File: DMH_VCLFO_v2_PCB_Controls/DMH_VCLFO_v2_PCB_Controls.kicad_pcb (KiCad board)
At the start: 2 copper layers, 98 x 120.5 mm, 67 parts, among them J19 Conn_01x08, J20 Conn_01x08, J24 Conn_01x08, J25 Conn_01x08, J29 Conn_01x08, J30 Conn_01x08, J54 Conn_01x06, Q1 BC548, Q2 BC558, Q3 BC548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

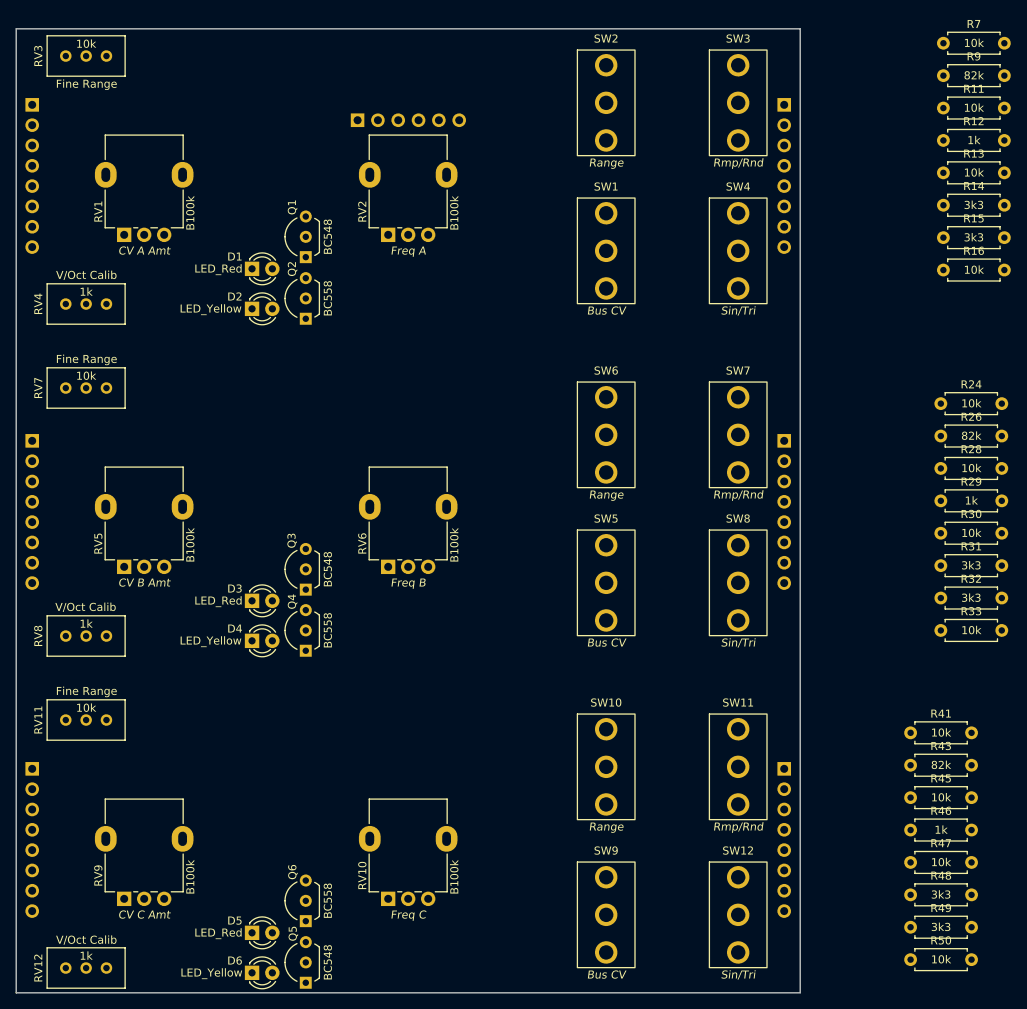
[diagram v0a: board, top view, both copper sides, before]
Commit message: Controls PCB routing done
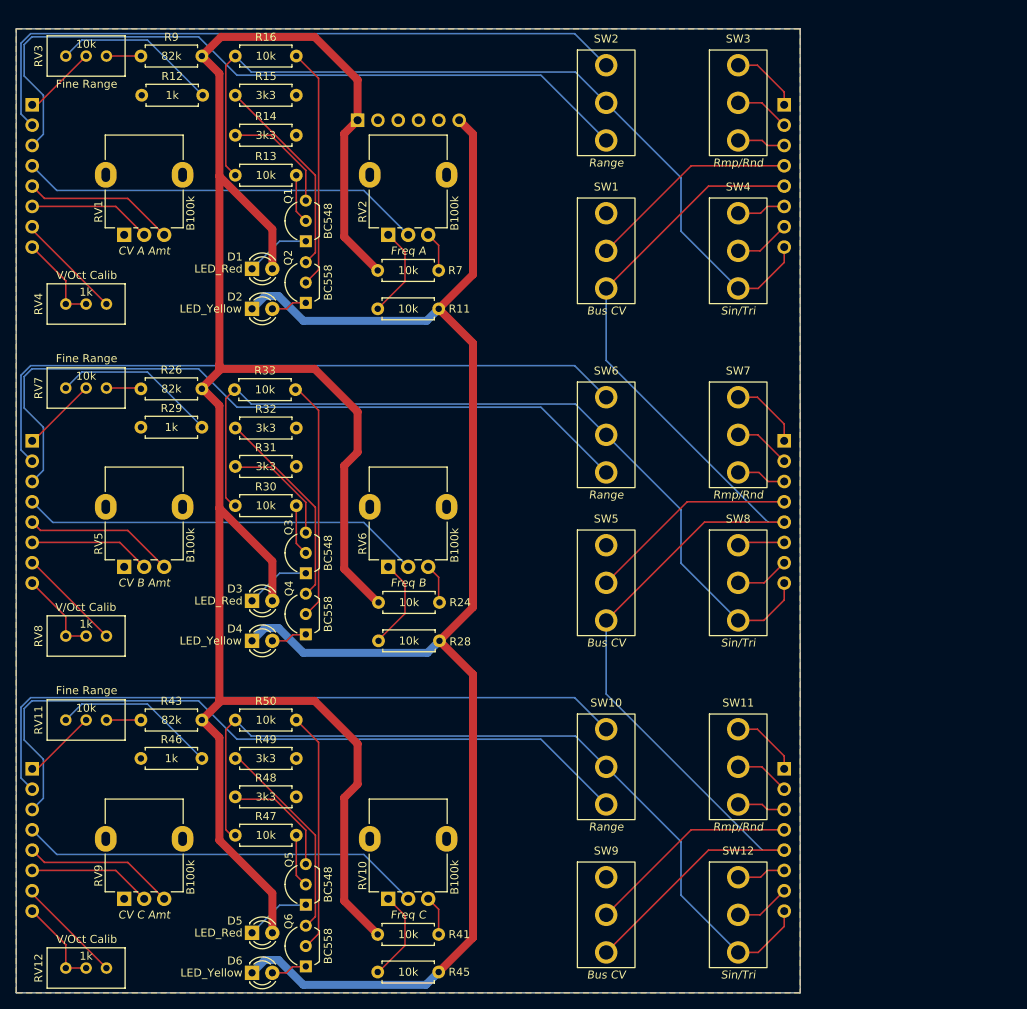
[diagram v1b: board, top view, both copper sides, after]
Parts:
- moved R29 100.4 mm to (66.6, 92.3)
- moved R12 100.4 mm to (66.7, 50.8)
- moved R9 100.3 mm to (66.6, 45.9)
- moved R26 100.2 mm to (66.6, 87.5)
- moved R46 96.6 mm to (66.6, 133.7)
- moved R43 96.4 mm to (66.6, 128.9)
- moved R33 93.3 mm to (78.3, 87.6)
- moved R16 92.5 mm to (78.4, 45.9)
- moved R32 90.7 mm to (78.4, 92.4)
- moved R15 90.3 mm to (78.4, 50.8)
- moved R50 89.6 mm to (78.4, 128.9)
- moved R31 89.1 mm to (78.4, 97.2)
- moved R14 88.9 mm to (78.4, 55.8)
- moved R13 88.5 mm to (78.4, 60.8)
- moved R30 88.3 mm to (78.4, 102.1)
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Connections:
- J19 pad 1: A_Rng_Sw_p1_C -> A_FRng_Trim_p2_C
- J19 pad 3: A_Freq_Pot_p2_C -> A_Rng_Sw_p1_C
- J19 pad 4: A_CV_Amt_Pot_p2_C -> A_Freq_Pot_p2_C
- J19 pad 6: A_FRng_Trim_p2_C -> A_CV_Amt_Pot_p2_C
- J19 pad 7: A_VOct_Trim_p12_C -> A_VOct_Trim_p3_C
- J19 pad 8: A_VOct_Trim_p3_C -> A_VOct_Trim_p12_C
- J20 pad 4: A_Sin_C -> A_BusCV_Sw_p2_C
- J20 pad 5: A_Sin_Tri_Sw_p2_C -> Bus_CV_C
- J20 pad 6: A_Tri_C -> A_Sin_C
- J20 pad 7: A_BusCV_Sw_p2_C -> A_Sin_Tri_Sw_p2_C
- J20 pad 8: Bus_CV_C -> A_Tri_C
- J24 pad 1: B_Rng_Sw_p1_C -> B_FRng_Trim_p2_C
- J24 pad 3: B_Freq_Pot_p2_C -> B_Rng_Sw_p1_C
- J24 pad 4: B_CV_Amt_Pot_p2_C -> B_Freq_Pot_p2_C
- J24 pad 6: B_FRng_Trim_p2_C -> B_CV_Amt_Pot_p2_C
- J24 pad 7: B_VOct_Trim_p12_C -> B_VOct_Trim_p3_C
- J24 pad 8: B_VOct_Trim_p3_C -> B_VOct_Trim_p12_C
- J25 pad 4: B_Sin_C -> B_BusCV_Sw_p2_C
- J25 pad 5: B_Sin_Tri_Sw_p2_C -> Bus_CV_C
- J25 pad 6: B_Tri_C -> B_Sin_C
- J25 pad 7: B_BusCV_Sw_p2_C -> B_Sin_Tri_Sw_p2_C
- J25 pad 8: Bus_CV_C -> B_Tri_C
- J29 pad 1: C_Rng_Sw_p1_C -> C_FRng_Trim_p2_C
- J29 pad 3: C_Freq_Pot_p2_C -> C_Rng_Sw_p1_C
- J29 pad 4: C_CV_Amt_Pot_p2_C -> C_Freq_Pot_p2_C
- J29 pad 6: C_FRng_Trim_p2_C -> C_CV_Amt_Pot_p2_C
- J29 pad 7: C_VOct_Trim_p12_C -> C_VOct_Trim_p3_C
- J29 pad 8: C_VOct_Trim_p3_C -> C_VOct_Trim_p12_C
- J30 pad 4: C_Sin_C -> C_BusCV_Sw_p2_C
- J30 pad 5: C_Sin_Tri_Sw_p2_C -> Bus_CV_C
- J30 pad 6: C_Tri_C -> C_Sin_C
- J30 pad 7: C_BusCV_Sw_p2_C -> C_Sin_Tri_Sw_p2_C
- J30 pad 8: Bus_CV_C -> C_Tri_C
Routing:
- net +12V: track 0.00 -> 286.5 mm
- net -12V: track 0.00 -> 193.8 mm
- net Bus_CV_C: track 0.00 -> 161.6 mm
- net B_Tri_C: track 0.00 -> 104.1 mm
- net A_Tri_C: track 0.00 -> 103.7 mm
- net C_Tri_C: track 0.00 -> 103.7 mm
- net B_Rng_Sw_p1_C: track 0.00 -> 93.2 mm
- net A_Rng_Sw_p1_C: track 0.00 -> 92.8 mm
- net C_Rng_Sw_p1_C: track 0.00 -> 92.8 mm
- net B_Rng_Sw_p3_C: track 0.00 -> 86.6 mm
- net A_Rng_Sw_p3_C: track 0.00 -> 86.1 mm
- net C_Rng_Sw_p3_C: track 0.00 -> 86.1 mm
- net C_Freq_Pot_p2_C: track 0.00 -> 50.6 mm
- net A_Freq_Pot_p2_C: track 0.00 -> 50.6 mm
- net B_Freq_Pot_p2_C: track 0.00 -> 50.4 mm
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- added copper zone on B.Cu, net GND
- added copper zone on F.Cu, net GND

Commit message: Generated Gerbers
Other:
- board text added: "Mk1.0 - March 2026"
- board text removed: "Mk1.0 - Month Year"
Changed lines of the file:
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@@
 			(plot_on_all_layers_selection 0x00000000_00000000_00000000_00000000)
 			(disableapertmacros no)
-			(usegerberextensions no)
+			(usegerberextensions yes)
 			(usegerberattributes yes)
 			(usegerberadvancedattributes yes)
@@
 			(sketchdnponfab yes)
 			(crossoutdnponfab yes)
-			(subtractmaskfromsilk no)
+			(subtractmaskfromsilk yes)
 			(outputformat 1)
 			(mirror no)
-			(drillshape 1)
+			(drillshape 0)
 			(scaleselection 1)
-			(outputdirectory "")
+			(outputdirectory "Gerbers/")
 		)
 	)
@@
 		(layer "User.9")
 	)
-	(gr_text "Mk1.0 - Month Year"
+	(gr_text "Mk1.0 - March 2026"
 		(at 114.9 162 0)
 		(layer "B.SilkS")
